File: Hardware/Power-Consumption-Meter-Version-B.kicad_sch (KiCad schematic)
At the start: 35 parts, among them J1 Jack_DC, J10 01x02, J11 01x02, J12 01x02, J13 01x02, J2 BAT_IN, J3 PWR_BTN, J4 USB_A, J5 Jack_DC, J6 Jack_DC, J7 USB_B_Mini, J8 USB_B_Micro, J9 01x04, SW1 SW_Slide, SW2 SW_Push, U1 Arduino_Nano_v3.x, U2 Display_5641BS, U3 INA219_Module

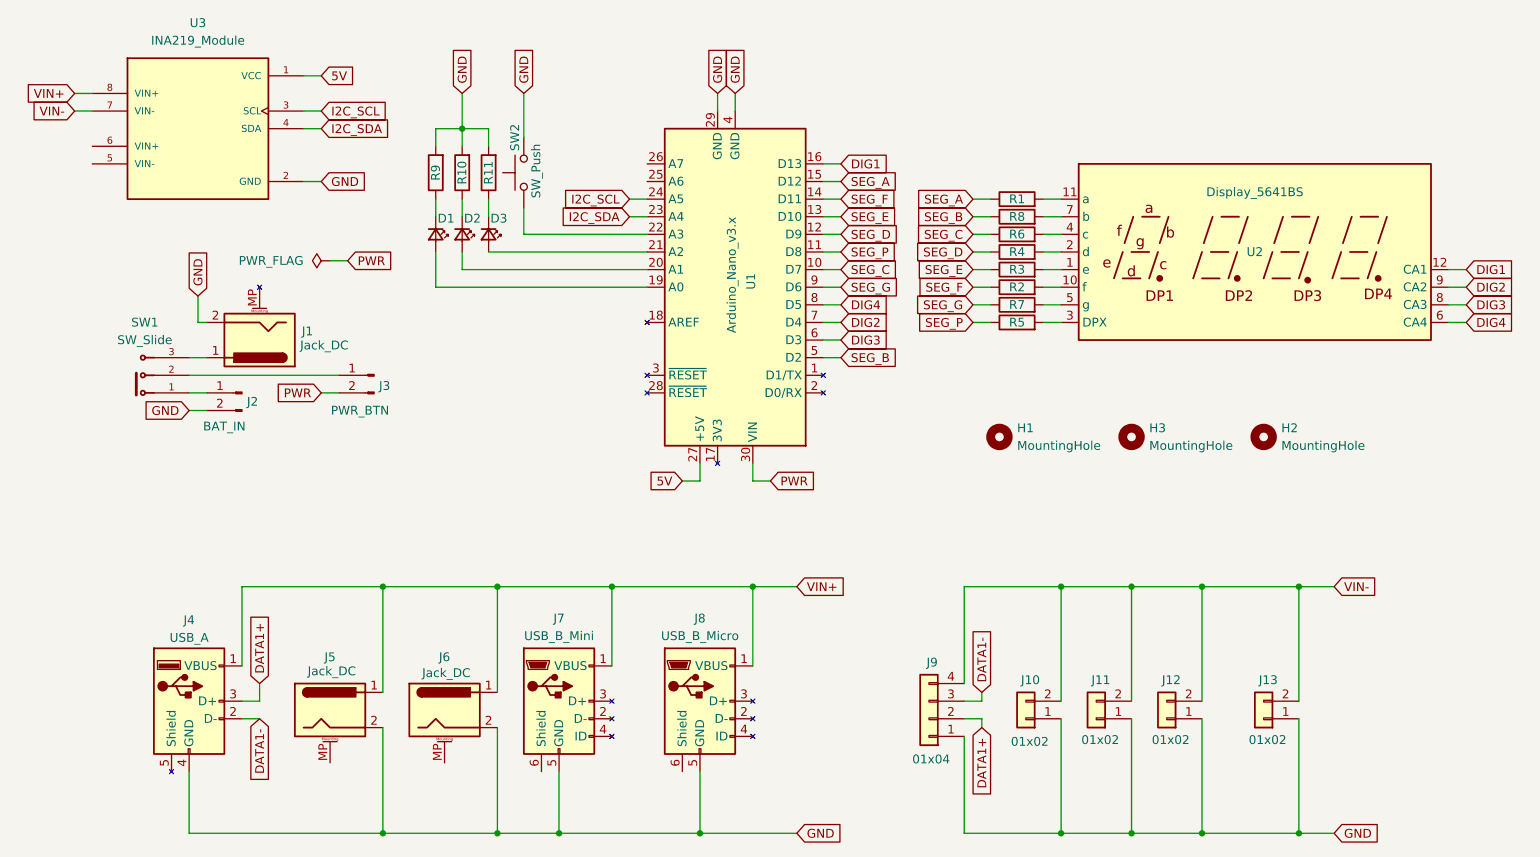
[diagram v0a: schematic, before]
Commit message: Version B: adding case 3D model
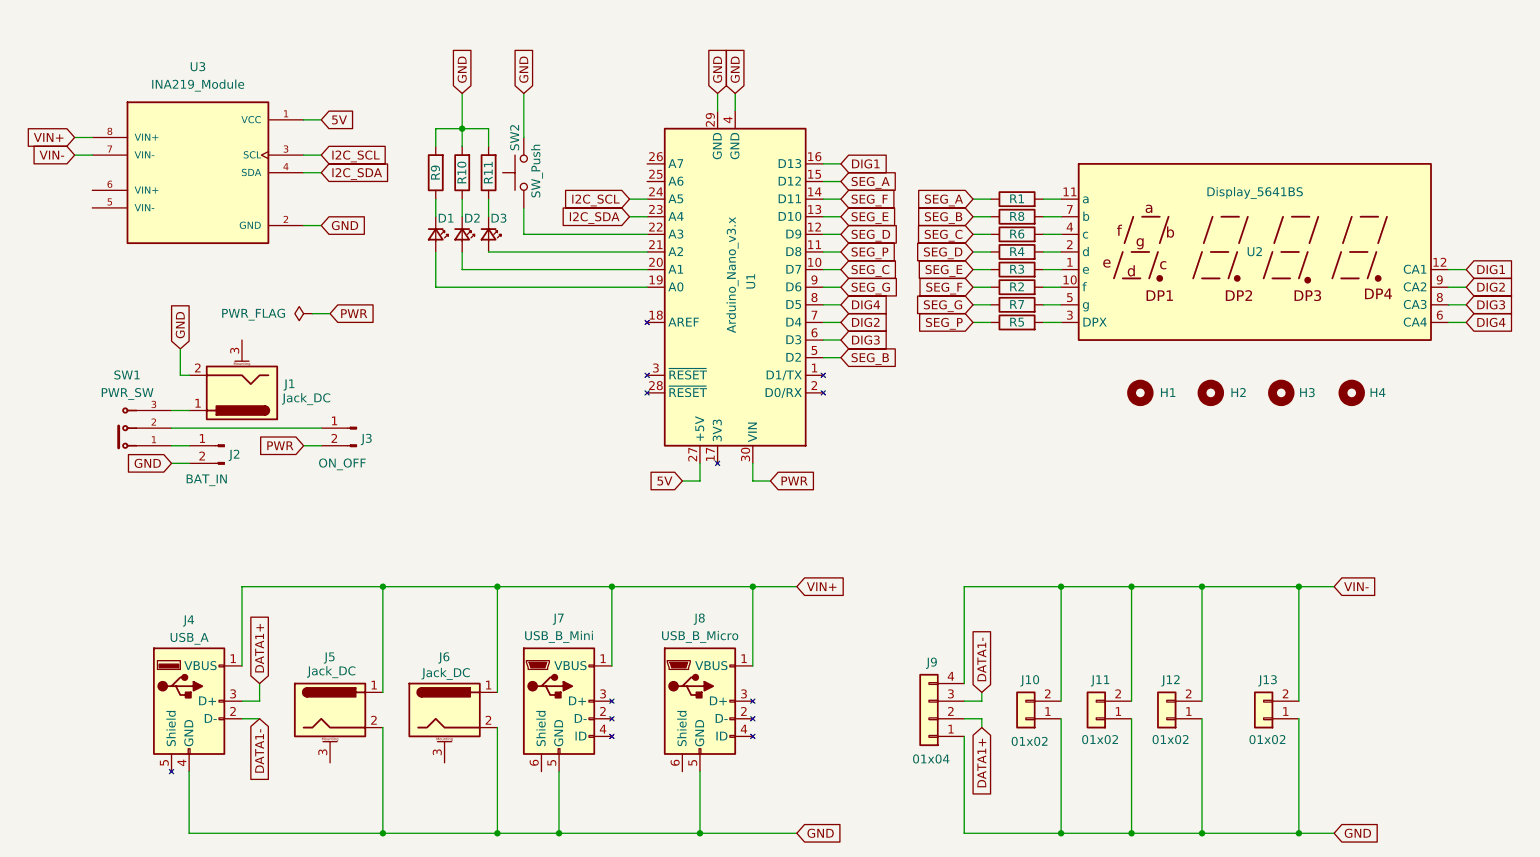
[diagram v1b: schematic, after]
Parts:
- added H4: MountingHole, MountingHole:MountingHole_2mm, symbol Mechanical:MountingHole
- J3: value PWR_BTN -> ON_OFF
- SW1: value SW_Slide -> PWR_SW
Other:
- moved on the sheet: H1, H2, H3, J2, J3, SW1, U3
